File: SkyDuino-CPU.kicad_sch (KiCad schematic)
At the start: 37 parts, among them J11 DBG, J12 USB-A RMT, J13 DISP, J14 USB_C Artisan, SW1 BOOT, U10 USBLC6-2SC6, U7 25MHz, U8 USBLC6-2SC6, U9 STM32F411RET6, Y1 32.768kHz

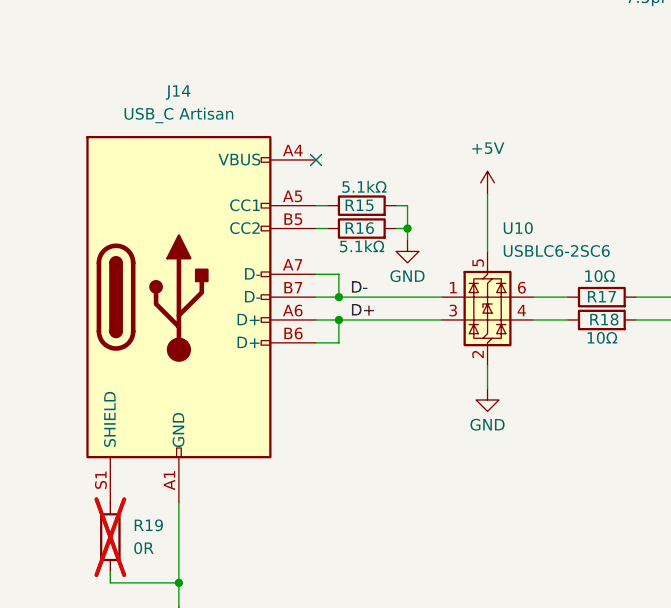
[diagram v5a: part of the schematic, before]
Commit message: Unhide USB-C rec VBUS pins
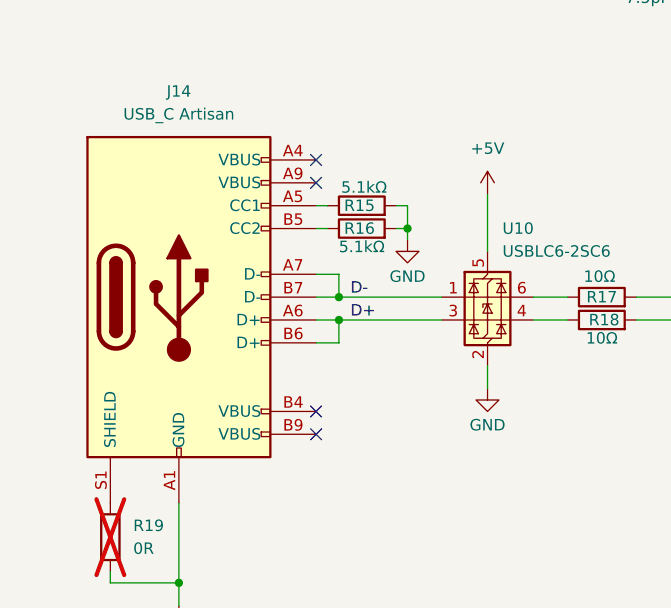
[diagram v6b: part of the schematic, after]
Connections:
- now unconnected: J14.A4 (VBUS), J14.A9 (VBUS), J14.B4 (VBUS), J14.B9 (VBUS)
- no-connect marks 31 -> 34
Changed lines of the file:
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@@
+	)
+	(no_connect
+		(at 45.72 172.72)
 	)
 	(no_connect
@@
 	)
 	(no_connect
+		(at 45.72 144.78)
+	)
+	(no_connect
 		(at 135.89 69.85)
 	)
@@
 	)
 	(no_connect
+		(at 45.72 170.18)
+	)
+	(no_connect

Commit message: update footprint for resistors to hand solder
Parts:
- R11, R9: footprint Resistor_SMD:R_0805_2012Metric -> Resistor_SMD:R_0805_2012Metric_Pad1.20x1.40mm_HandSolder
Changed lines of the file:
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@@
 			)
 		)
-		(property "Footprint" "Resistor_SMD:R_0805_2012Metric"
+		(property "Footprint" "Resistor_SMD:R_0805_2012Metric_Pad1.20x1.40mm_HandSolder"
 			(at 97.79 38.608 90)
 			(effects
@@
 			)
 		)
-		(property "Footprint" "Resistor_SMD:R_0805_2012Metric"
+		(property "Footprint" "Resistor_SMD:R_0805_2012Metric_Pad1.20x1.40mm_HandSolder"
 			(at 97.79 33.528 90)
 			(effects
